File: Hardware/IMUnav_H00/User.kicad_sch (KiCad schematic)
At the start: 10 parts, among them SW2 SW_SPST, SW3 SW_SPST, SW4 SW_SPST, SW5 SW_SPST, U11 OLED_I2C

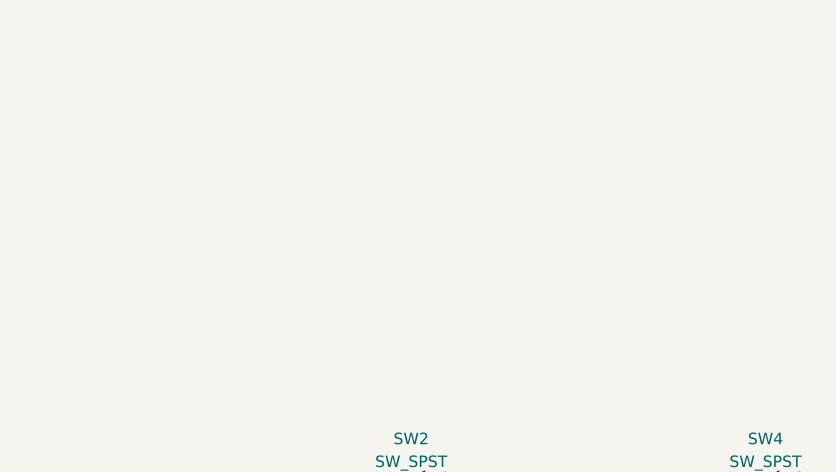
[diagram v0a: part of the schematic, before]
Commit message: Added signal connections to MCU+misc
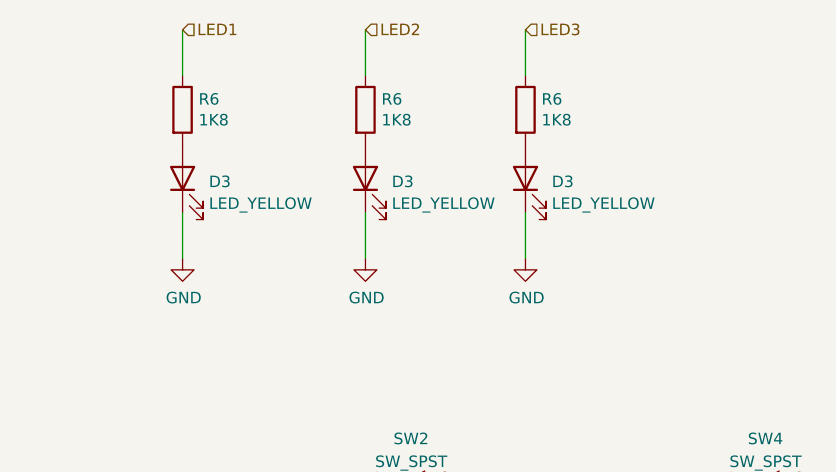
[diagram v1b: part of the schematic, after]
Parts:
- added D3 (x3): LED_YELLOW, LED_SMD:LED_0603_1608Metric, symbol Device:LED
- added R6 (x3): 1K8, Resistor_SMD:R_0603_1608Metric, symbol Device:R
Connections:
- net GND: now also D3.1 (K), D3.1 (K), D3.1 (K)
- new net: D3.2 (A), R6.2 (x3)
- new net LED1: R6.1
- new net LED2: R6.1
- new net LED3: R6.1

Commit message: Thesis - added appendix
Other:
- note added: "Navigation push button"
- note added: "OLED"
- note added: "Status LED"
- title: (none) -> IMUnav
- moved on the sheet: C45, SW2, SW3, SW4, SW5, U11
